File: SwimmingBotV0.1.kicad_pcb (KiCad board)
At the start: 2 copper layers, 70 x 51 mm, 137 parts, among them P10 ANT, P11 DEBUG, P2 ANALOG, P3 CHRG, P4 BATT, P5 DEBUG_JUMPER, P6 FIN1, P7 FIN2, P8 MOT1, P9 MOT2, Q1 Q_NMOS_DGS, Q10 PMV45EN2, Q11 PMV45EN2, Q12 PMV45EN2, Q13 PMV45EN2, Q14 PMV45EN2, Q15 PMV45EN2, Q2 Q_PMOS_DGS, Q3 Q_NMOS_DGS, Q4 PMV45EN2, Q5 PMV45EN2, Q6 PMV45EN2, Q7 PMV45EN2, Q8 PMV45EN2, Q9 PMV45EN2, U1 LT3470A, U10 TPS6216X, U2 MCP73834, U3 A4960, U4 A4960, U5 HUM-900-PRO, U6 MPU-9250, U8 MAX6034_25, U9 STM32F446-144, X1 CRYSTAL_SMD, Y1 Crystal

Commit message: potentially done with parts removal and reselection, on to pcb layout
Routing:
- net /Power/AUX_3.3V_EN: track 49.5 -> 37.4 mm, vias 3 -> 2
- net /Micro/PG12: track 41.8 -> 39.2 mm

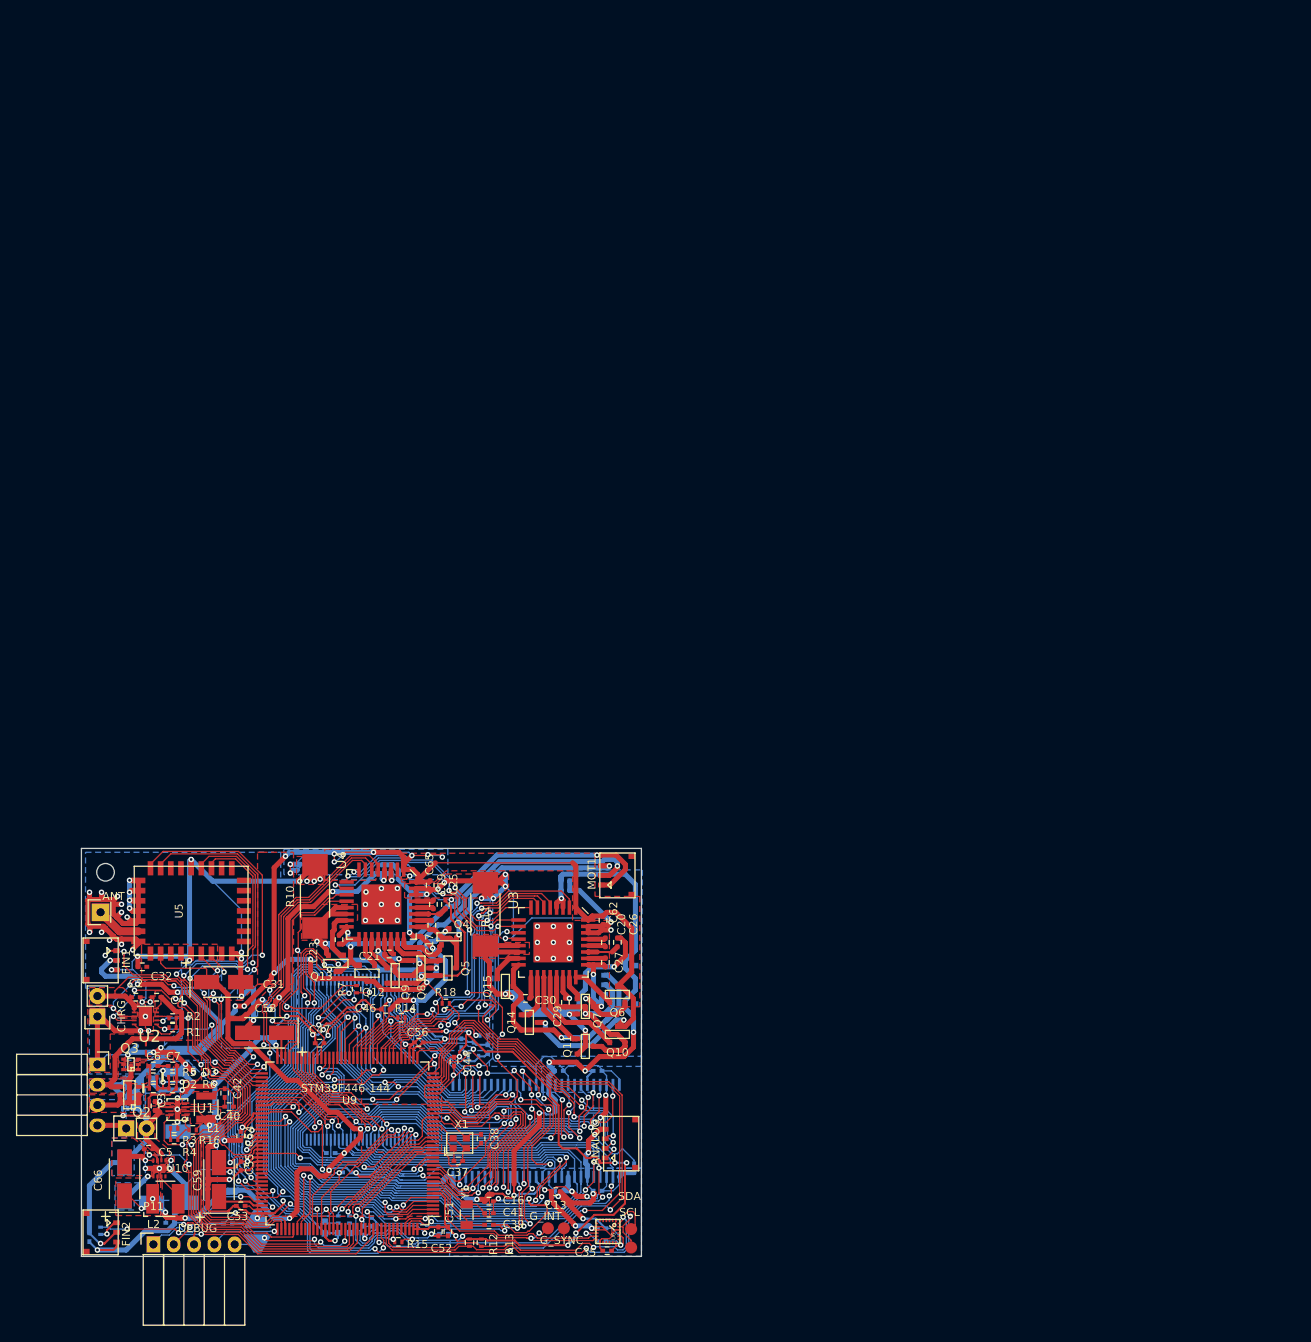
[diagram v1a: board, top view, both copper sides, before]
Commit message: swapped v0.2 pcb to v0.1 pcb since kicad doesn't like different file names
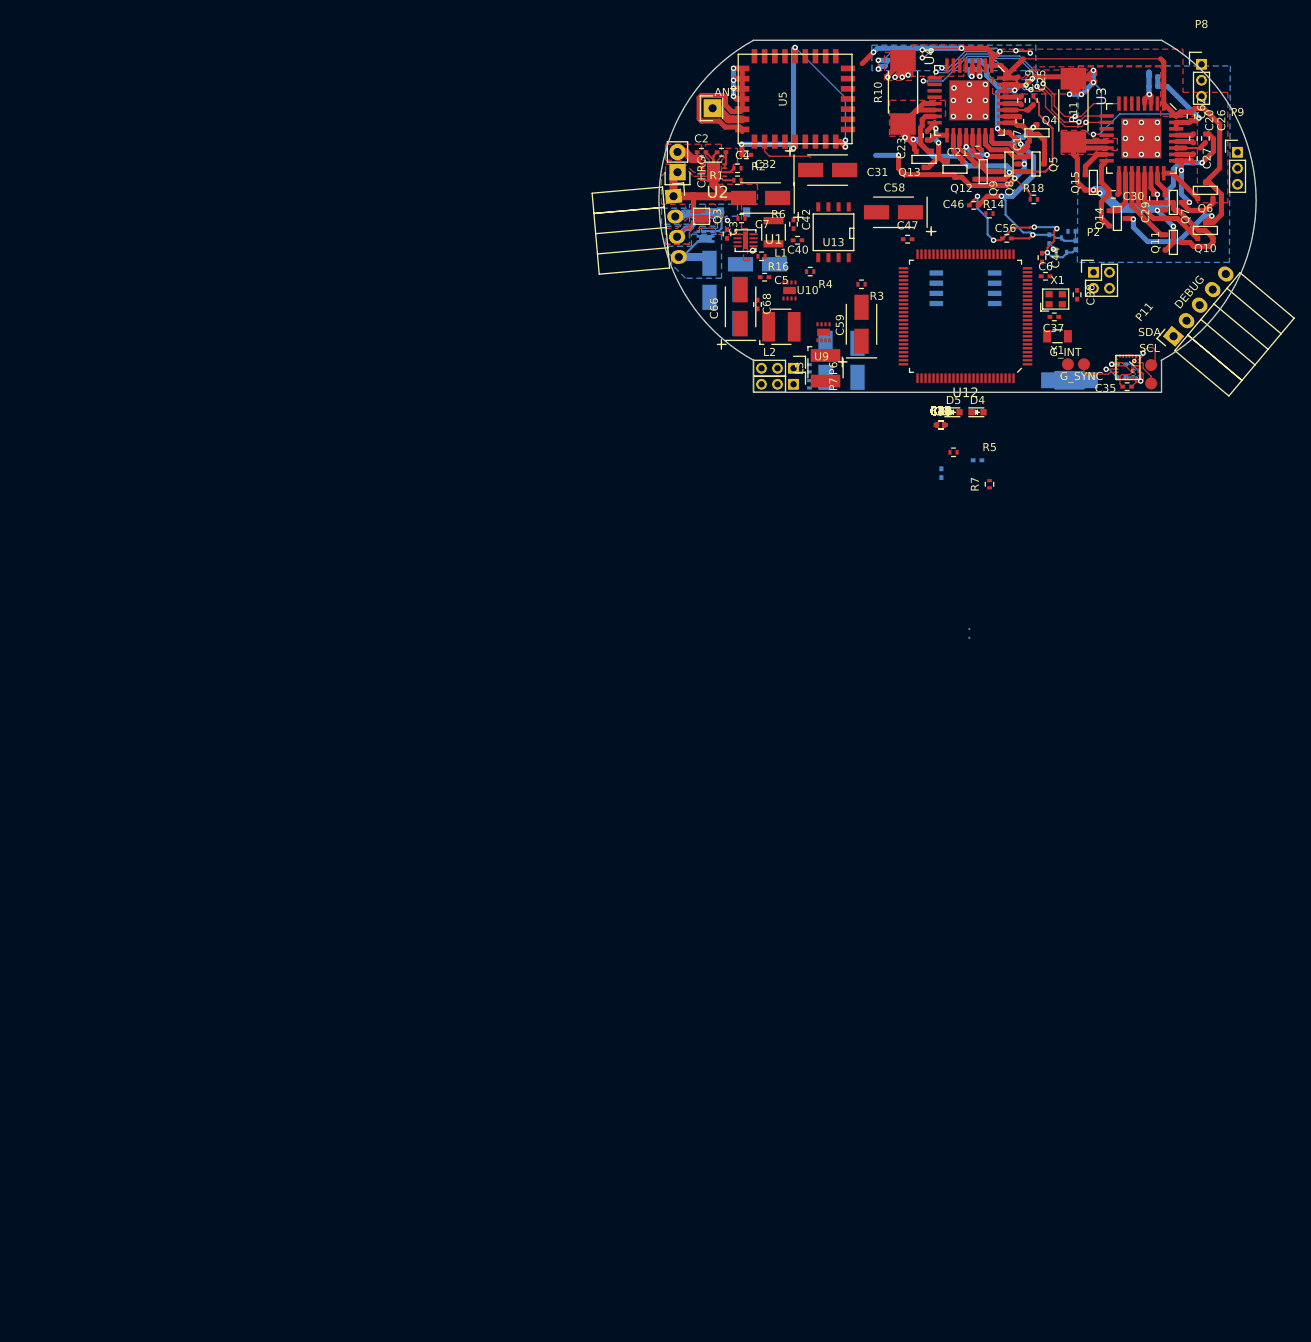
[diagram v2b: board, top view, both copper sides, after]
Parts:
- removed C13, C14, C15, C16, C52, C53, C54, C55, C57: 100nF, Capacitors_SMD:C_0402
- removed C64, C65: 1uF, Capacitors_SMD:C_0402
- removed D2, D3: D_Schottky, Custom_Footprints:D_0402_SOD_923
- removed MEM1: IS42S16160G, Custom_Footprints:TSOP-54
- removed MEM2: S29GL256S, Custom_Footprints:TSOP-56_TYPE_1
- removed P5: DEBUG_JUMPER, Socket_Strips:Socket_Strip_Straight_1x02
- removed REF**: MountingHole_2.2mm_M2, Mounting_Holes:MountingHole_2.2mm_M2
- added C36, C48: 100nF, Capacitors_SMD:C_0402, F.Cu at (119.4, 94.1)
- added L3: 2.2uH, Inductors:NR4018, F.Cu at (105.0, 87.0)
- added R21, R22, R23: 10k, Resistors_SMD:R_0402, F.Cu at (119.4, 94.1)
- added U11: SST26VF064B, Housings_SOIC:SOIJ-8_5.3x5.3mm_Pitch1.27mm, B.Cu at (122.5, 77.0)
- added U12: STM32F446-100, Custom_Footprints:STM32F446_QFP_100, F.Cu at (122.5, 80.5)
- added U13: LTC1163, SMD_Packages:SOIC-8-N, F.Cu at (106.0, 70.0)
- C10, C11: value 100nF -> 10uF; footprint Capacitors_SMD:C_0402 -> Capacitors_Tantalum_SMD:TantalC_SizeB_EIA-3528_HandSoldering
- C12: value 100nF -> 1uF; moved to F.Cu
- C49, C50, C68, C8, C9, D4, D5, R17, R20: moved to F.Cu
- C6: value 1nF -> 1uF
- C7: value 1nF -> 10uF; footprint Capacitors_SMD:C_0402 -> Capacitors_Tantalum_SMD:TantalC_SizeB_EIA-3528_HandSoldering
- JP1: footprint Custom_Footprints:JUMPER -> Oddities:NetTie-I_Connected_SMD
- P2: footprint Custom_Footprints:PICO-EZMATE-4 -> Pin_Headers:Pin_Header_Straight_2x02_Pitch2.00mm
- P6, P7, P8: footprint Custom_Footprints:PICO-EZMATE-3 -> Pin_Headers:Pin_Header_Straight_1x03_Pitch2.00mm
- P9: footprint Custom_Footprints:PICO-EZMATE-3 -> Pin_Headers:Pin_Header_Straight_1x03_Pitch2.00mm; moved to F.Cu
- Q1, Q3: footprint Custom_Footprints:SC-70-6-DGS -> Custom_Footprints:SC-70-ENHANCED-DGS
- Q2: value Q_PMOS_DGS -> Q_NMOS_DGS; footprint Custom_Footprints:TSOP-6_Si3407DV -> Custom_Footprints:SC-70-ENHANCED-DGS; moved to B.Cu
- R1: value 10k -> 5k
- R19: value 10k -> 4.1k-3.9k
- R5: value 10k -> 65k
- U9: value STM32F446-144 -> TPS6216X; footprint Housings_QFP:LQFP-144_20x20mm_Pitch0.5mm -> Custom_Footprints:WSON-8
- moved P11 170.7 mm to (148.5, 83.0), turned to 50 degrees
- moved C6 148.9 mm to (132.5, 75.5)
- moved JP1 147.0 mm to (135.5, 88.5), turned to 180 degrees
- moved C63 143.0 mm to (119.5, 100.1)
- moved R9 138.0 mm to (103.0, 89.0)
- moved C68 136.3 mm to (96.5, 79.0), turned to 90 degrees
- moved R3 136.1 mm to (109.5, 76.5)
- moved P7 135.9 mm to (101.0, 89.0)
- moved U10 135.1 mm to (100.8, 77.3)
- moved R4 134.5 mm to (103.1, 74.9)
- moved C1 134.1 mm to (90.5, 76.0)
- moved C59 133.7 mm to (109.5, 81.5)
- moved C60 133.7 mm to (124.0, 98.5)
- moved C5 133.5 mm to (97.4, 75.6)
- moved C66 133.5 mm to (94.4, 79.3)
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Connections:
- C10 pad 1: GND -> /Motors/VFIN
- C10 pad 2: /Digital/3.3V -> GND
- C11 pad 1: GND -> /Motors/VFIN
- C11 pad 2: /Digital/3.3V -> GND
- C12 pad 2: /Digital/3.3V -> /Motors/VFIN
- C6 pad 1: Net-(C6-Pad1) -> /Micro/A0
- C7 pad 1: Net-(C7-Pad1) -> /Charge/2S
- C9 pad 1: GND -> /Charge/2S
- C9 pad 2: /Digital/3.3V -> GND
- P4 pad 4: /Charge/2S_RAW -> /Charge/2S
- P6 pad 2: /Charge/2S -> /Motors/VFIN
- P7 pad 2: /Charge/2S -> /Motors/VFIN
- Q1 pad 2: Net-(C7-Pad1) -> /Charge/GATE2
- Q2 pad 1: /Charge/2S_NEG -> /Charge/1S
- Q2 pad 2: Net-(C6-Pad1) -> /Charge/GATE3
- Q2 pad 3: /Charge/1S -> /Charge/2S_NEG
- Q3 pad 2: Net-(C7-Pad1) -> /Charge/GATE1
- R1 pad 2: GND -> Net-(R1-Pad2)
- R14 pad 1: /Micro/SDIO_CLK -> /Charge/5V_CHG
- R14 pad 2: GND -> Net-(R14-Pad2)
- R17 pad 2: /Micro/PF7 -> /Micro/PD14
- R20 pad 2: /Micro/PF8 -> /Micro/PE3
- R5 pad 1: /Charge/2S_EN -> /Motors/VFIN
- R5 pad 2: Net-(C6-Pad1) -> Net-(R5-Pad2)
- R6 pad 1: /Charge/2S_EN -> GND
- R6 pad 2: Net-(C7-Pad1) -> Net-(R5-Pad2)
- R7 pad 1: /Micro/FMC_NWAIT -> /Charge/1S
- R7 pad 2: /Digital/3.3V -> /Micro/PA8
- U1 pad 7: Net-(U1-Pad7) -> (no net)
- U1 pad 8: /Micro/PG12 -> /Micro/PA8
- U2 pad 6: /Charge/CHG_EN# -> Net-(R1-Pad2)
- U2 pad 7: /Charge/CHG_TE# -> Net-(R14-Pad2)
- U3 pad PAD: Net-(U3-PadPAD) -> (no net)
- U4 pad PAD: Net-(U4-PadPAD) -> (no net)
- U5 pad 1: Net-(U5-Pad1) -> (no net)
- U5 pad 10: Net-(U5-Pad10) -> (no net)
- U5 pad 11: Net-(U5-Pad11) -> (no net)
- U5 pad 12: /Micro/PG7 -> /Micro/PD15
- U5 pad 13: /Micro/PG6 -> /Micro/PE1
- U5 pad 2: Net-(U5-Pad2) -> (no net)
- U5 pad 23: Net-(U5-Pad23) -> (no net)
- U5 pad 24: Net-(U5-Pad24) -> (no net)
- U5 pad 28: Net-(U5-Pad28) -> /rf/RF_CTS
- U5 pad 3: Net-(U5-Pad3) -> (no net)
- U5 pad 30: Net-(U5-Pad30) -> (no net)
- U5 pad 31: Net-(U5-Pad31) -> /Micro/PE13
- U5 pad 32: Net-(U5-Pad32) -> (no net)
- U5 pad 4: Net-(U5-Pad4) -> (no net)
- U5 pad 5: Net-(U5-Pad5) -> (no net)
- U5 pad 6: Net-(U5-Pad6) -> (no net)
- U6 pad 14: Net-(U6-Pad14) -> (no net)
- U6 pad 15: Net-(U6-Pad15) -> (no net)
- U6 pad 16: Net-(U6-Pad16) -> (no net)
- U6 pad 17: Net-(U6-Pad17) -> (no net)
- U6 pad 19: Net-(U6-Pad19) -> (no net)
- U6 pad 2: Net-(U6-Pad2) -> (no net)
- U6 pad 21: /Sensors/AUX_SDA -> (no net)
- U6 pad 3: Net-(U6-Pad3) -> (no net)
- U6 pad 4: Net-(U6-Pad4) -> (no net)
- U6 pad 5: Net-(U6-Pad5) -> (no net)
- U6 pad 6: Net-(U6-Pad6) -> (no net)
- U6 pad 7: /Sensors/AUX_SCL -> (no net)
- U9 pad 1: /Digital/A23 -> GND
- U9 pad 2: /Digital/A19 -> /Charge/2S
- U9 pad 3: /Digital/A20 -> /Micro/PD0
- U9 pad 4: /Digital/A21 -> GND
- U9 pad 5: /Digital/A22 -> Net-(R5-Pad2)
- U9 pad 6: /Power/CHG_CTL_VCC -> /Motors/VFIN
- U9 pad 7: /Sensors/GYRO_FSYNC -> Net-(L3-Pad2)
- U9 pad 8: /Micro/X1 -> /Micro/PD1
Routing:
- net GND: track 642.9 -> 222.1 mm, vias 90 -> 27
- net /Digital/3.3V: track 310.0 -> 31.5 mm, vias 29 -> 4
- net /Power/CHG_CTL_VCC: track 266.3 -> 25.0 mm, vias 27 -> 5
- net /Charge/2S: track 280.5 -> 170.2 mm, vias 23 -> 16
- net /Motors/MOT2_TACH: track 109.4 -> 0.67 mm, vias 6 -> 0
- net /Digital/DQ5: track 93.1 -> 0.00 mm, vias 3 -> 0
- net /Digital/DQ4: track 92.0 -> 0.00 mm, vias 1 -> 0
- net /Digital/DQ6: track 91.0 -> 0.00 mm, vias 3 -> 0
- net /Digital/DQ0: track 89.1 -> 0.00 mm, vias 3 -> 0
- net /Digital/DQ1: track 88.6 -> 0.00 mm, vias 3 -> 0
- net /Motors/SDO: track 112.7 -> 28.9 mm, vias 6 -> 3
- net /Digital/DQ2: track 82.1 -> 0.00 mm, vias 3 -> 0
- net /Digital/A15: track 81.6 -> 0.00 mm, vias 3 -> 0
- net /Digital/A14: track 81.3 -> 0.00 mm, vias 3 -> 0
- net /Micro/MOT1_PWM: track 79.2 -> 0.67 mm, vias 2 -> 0
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- added copper zone on B.Cu, net /Charge/2S_NEG
- removed copper zone on F.Cu, net /Power/CHG_CTL_VCC
- removed copper zone on F.Cu, net Net-(C40-Pad1)
- removed copper zone on F.Cu, net Net-(L2-Pad2)
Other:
- board size 70 x 51 mm -> 74.7 x 44 mm

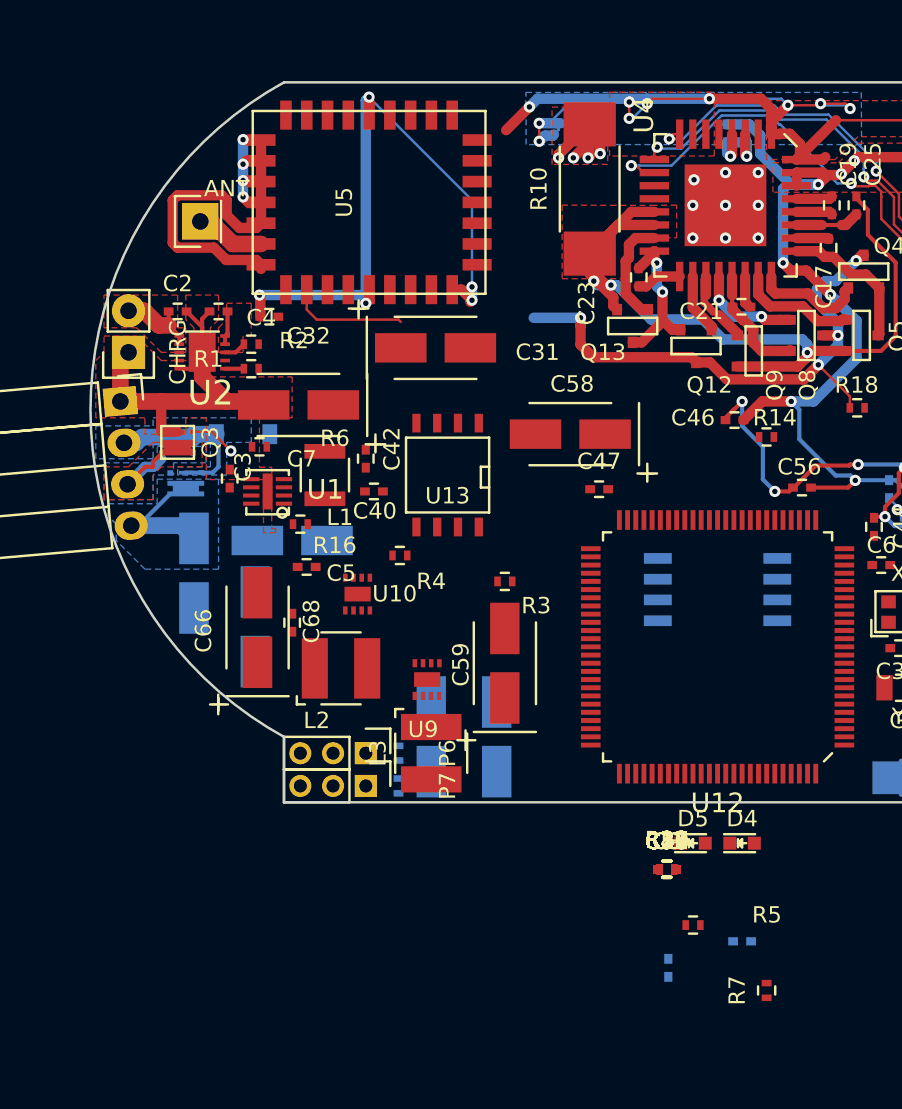
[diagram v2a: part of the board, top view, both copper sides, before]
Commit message: some pin swaps for routing, done with power section
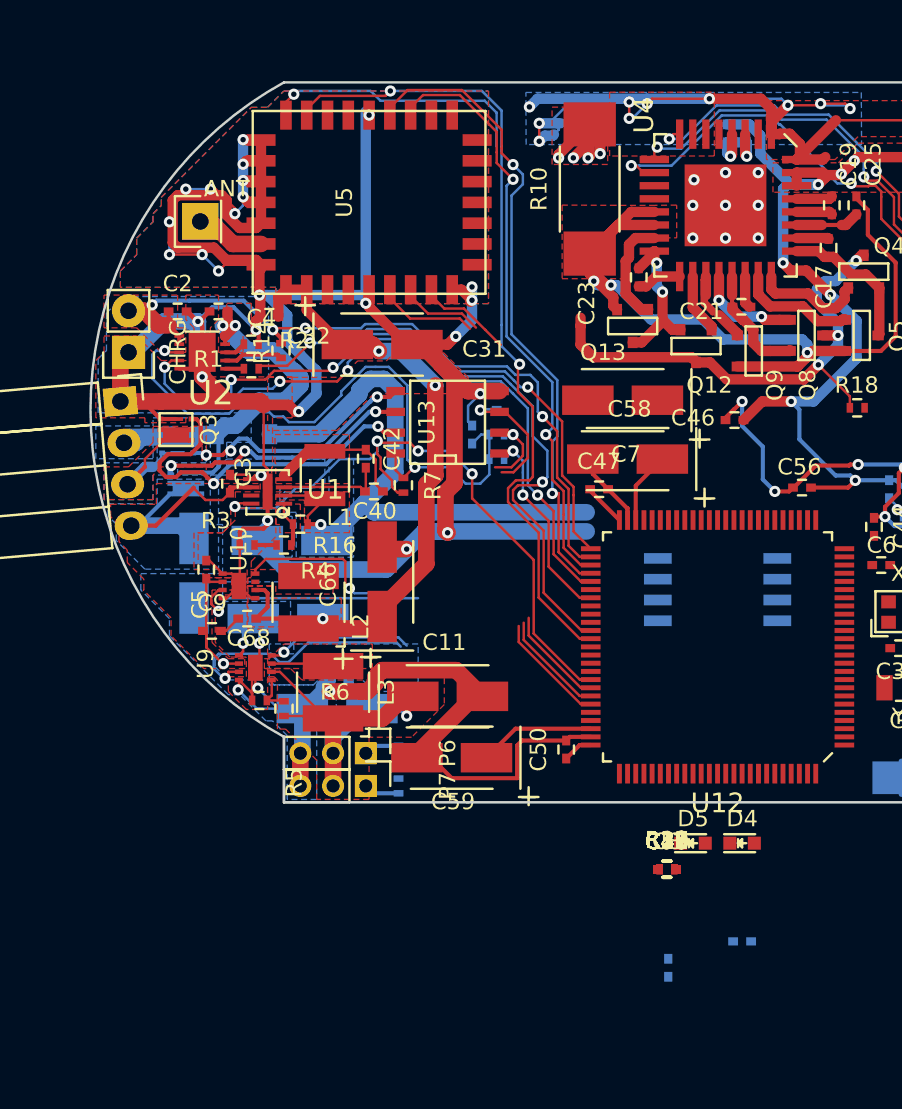
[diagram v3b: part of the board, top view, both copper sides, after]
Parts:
- added C13: 100nF, Capacitors_SMD:C_0402, B.Cu at (107.5, 67.5)
- C11: moved to F.Cu
- C12, R21, R22, R23: moved to B.Cu
- moved R7 38.0 mm to (103.3, 70.6), turned to 270 degrees
- moved C9 31.4 mm to (91.6, 79.5)
- moved R23 30.4 mm to (109.0, 65.5), turned to 270 degrees
- moved R14 30.1 mm to (95.8, 62.4), turned to 270 degrees
- moved R21 28.5 mm to (109.0, 67.5), turned to 180 degrees
- moved R5 28.3 mm to (96.0, 84.3), turned to 90 degrees
- moved R22 27.1 mm to (109.0, 69.0), turned to 180 degrees
- moved C12 23.6 mm to (99.4, 81.6)
- moved C7 19.8 mm to (116.7, 65.4)
- moved R3 15.9 mm to (93.8, 74.3), turned to 180 degrees
- moved R6 15.5 mm to (94.5, 83.8)
- moved U9 10.3 mm to (94.3, 81.5), turned to 270 degrees
- moved C50 9.56 mm to (113.3, 86.8), turned to 90 degrees
- moved C66 8.11 mm to (102.0, 76.5)
- moved U10 7.54 mm to (93.3, 76.5), turned to 270 degrees
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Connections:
- R17 pad 2: /Micro/PD14 -> /Micro/PE7
- U1 pad 7: (no net) -> Net-(U1-Pad7)
- U12 pad 15: /Charge/CHG_STAT2 -> /Micro/PC0
- U12 pad 17: (no net) -> /Micro/PC2
- U12 pad 29: (no net) -> /Micro/DCMI_HSYNC
- U12 pad 3: (no net) -> /Micro/DCMI_D4
- U12 pad 31: (no net) -> /Micro/DCMI_PIXCLK
- U12 pad 34: (no net) -> /Micro/PC5
- U12 pad 35: (no net) -> /Micro/SDIO_D1
- U12 pad 38: (no net) -> /Micro/PE7
- U12 pad 39: (no net) -> /Micro/PE8
- U12 pad 4: (no net) -> /Micro/DCMI_D6
- U12 pad 46: (no net) -> /Micro/PE15
- U12 pad 5: (no net) -> /Micro/DCMI_D7
- U12 pad 61: /Micro/PD14 -> /Charge/CHG_STAT2
- U12 pad 63: (no net) -> /Micro/DCMI_D0
- U12 pad 64: (no net) -> /Micro/DCMI_D1
- U12 pad 65: (no net) -> /Micro/SDIO_D0
- U12 pad 66: (no net) -> /Micro/DCMI_D3
- U12 pad 7: (no net) -> /Micro/PC13
- U12 pad 78: (no net) -> /Micro/SDIO_D2
- U12 pad 79: (no net) -> /Micro/SDIO_D3
- U12 pad 80: (no net) -> /Micro/SDIO_CLK
- U12 pad 83: (no net) -> /Micro/SDIO_CMD
- U12 pad 84: (no net) -> /Micro/DCMI_D5
- U12 pad 87: (no net) -> /Micro/PD6
- U12 pad 93: (no net) -> /Micro/DCMI_VSYNC
- U12 pad 97: (no net) -> /Micro/DCMI_D2
- U3 pad PAD: (no net) -> Net-(U3-PadPAD)
- U4 pad PAD: (no net) -> Net-(U4-PadPAD)
- U5 pad 1: (no net) -> Net-(U5-Pad1)
- U5 pad 10: (no net) -> Net-(U5-Pad10)
- U5 pad 11: (no net) -> Net-(U5-Pad11)
- U5 pad 2: (no net) -> Net-(U5-Pad2)
- U5 pad 23: (no net) -> Net-(U5-Pad23)
- U5 pad 24: (no net) -> Net-(U5-Pad24)
- U5 pad 3: (no net) -> Net-(U5-Pad3)
- U5 pad 30: (no net) -> /rf/RF_ACTV
- U5 pad 32: (no net) -> Net-(U5-Pad32)
- U5 pad 4: (no net) -> Net-(U5-Pad4)
- U5 pad 5: (no net) -> Net-(U5-Pad5)
- U5 pad 6: (no net) -> Net-(U5-Pad6)
- U6 pad 14: (no net) -> Net-(U6-Pad14)
- U6 pad 15: (no net) -> Net-(U6-Pad15)
- U6 pad 16: (no net) -> Net-(U6-Pad16)
- U6 pad 17: (no net) -> Net-(U6-Pad17)
- U6 pad 19: (no net) -> Net-(U6-Pad19)
- U6 pad 2: (no net) -> Net-(U6-Pad2)
- U6 pad 21: (no net) -> /Sensors/AUX_SDA
- U6 pad 3: (no net) -> Net-(U6-Pad3)
- U6 pad 4: (no net) -> Net-(U6-Pad4)
- U6 pad 5: (no net) -> Net-(U6-Pad5)
- U6 pad 6: (no net) -> Net-(U6-Pad6)
- U6 pad 7: (no net) -> /Sensors/AUX_SCL
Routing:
- net GND: track 222.1 -> 395.5 mm, vias 27 -> 49
- net /Micro/PD15: track 0.53 -> 50.6 mm, vias 0 -> 2
- net /Charge/CHG_STAT2: track 0.00 -> 47.8 mm, vias 0 -> 4
- net /Charge/1S: track 17.4 -> 64.1 mm, vias 0 -> 3
- net /Power/CHG_CTL_VCC: track 25.0 -> 70.2 mm, vias 5 -> 6
- net /Charge/CHG_STAT1: track 0.00 -> 44.0 mm, vias 0 -> 4
- net /Charge/5V_CHG: track 5.09 -> 46.1 mm, vias 0 -> 4
- net /Micro/PB15: track 0.53 -> 40.1 mm, vias 0 -> 2
- net /Micro/PA8: track 0.00 -> 38.5 mm, vias 0 -> 4
- net /Micro/PB14: track 0.68 -> 37.5 mm, vias 0 -> 2
- net /Digital/3.3V: track 31.5 -> 65.9 mm, vias 4 -> 7
- net /Charge/CHG_EN#: track 0.00 -> 30.4 mm, vias 0 -> 2
- net /Motors/VFIN: track 0.00 -> 28.5 mm, vias 0 -> 1
- net /Charge/GATE1: track 2.79 -> 22.1 mm, vias 1 -> 2
- net /Micro/PE1: track 0.53 -> 17.1 mm, vias 0 -> 1
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- added copper zone on F.Cu, net /Motors/VFIN
- added copper zone on B.Cu, net /Power/CHG_CTL_VCC
- added copper zone on F.Cu, net /Power/CHG_CTL_VCC
- added copper zone on F.Cu, net Net-(C40-Pad1)
- added copper zone on F.Cu, net Net-(L2-Pad2)
- added copper zone on F.Cu, net Net-(L3-Pad2)
- added copper zone on F.Cu, net Net-(R16-Pad2)
